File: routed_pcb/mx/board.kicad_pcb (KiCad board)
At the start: 2 copper layers, 100 x 100 mm, 28 parts

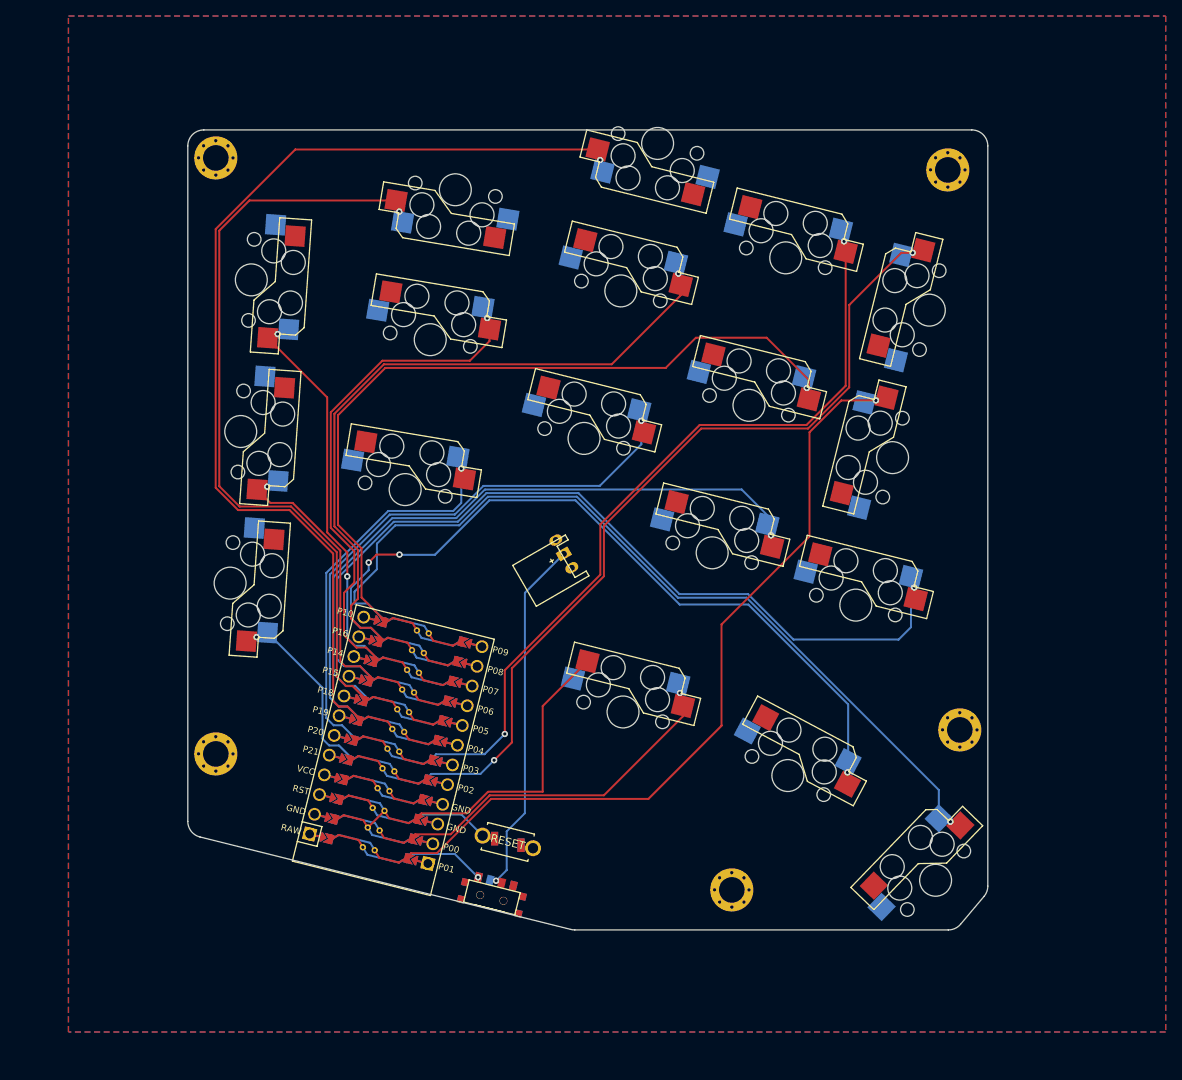
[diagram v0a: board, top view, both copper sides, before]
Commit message: choc v1.1 and mx v1.2
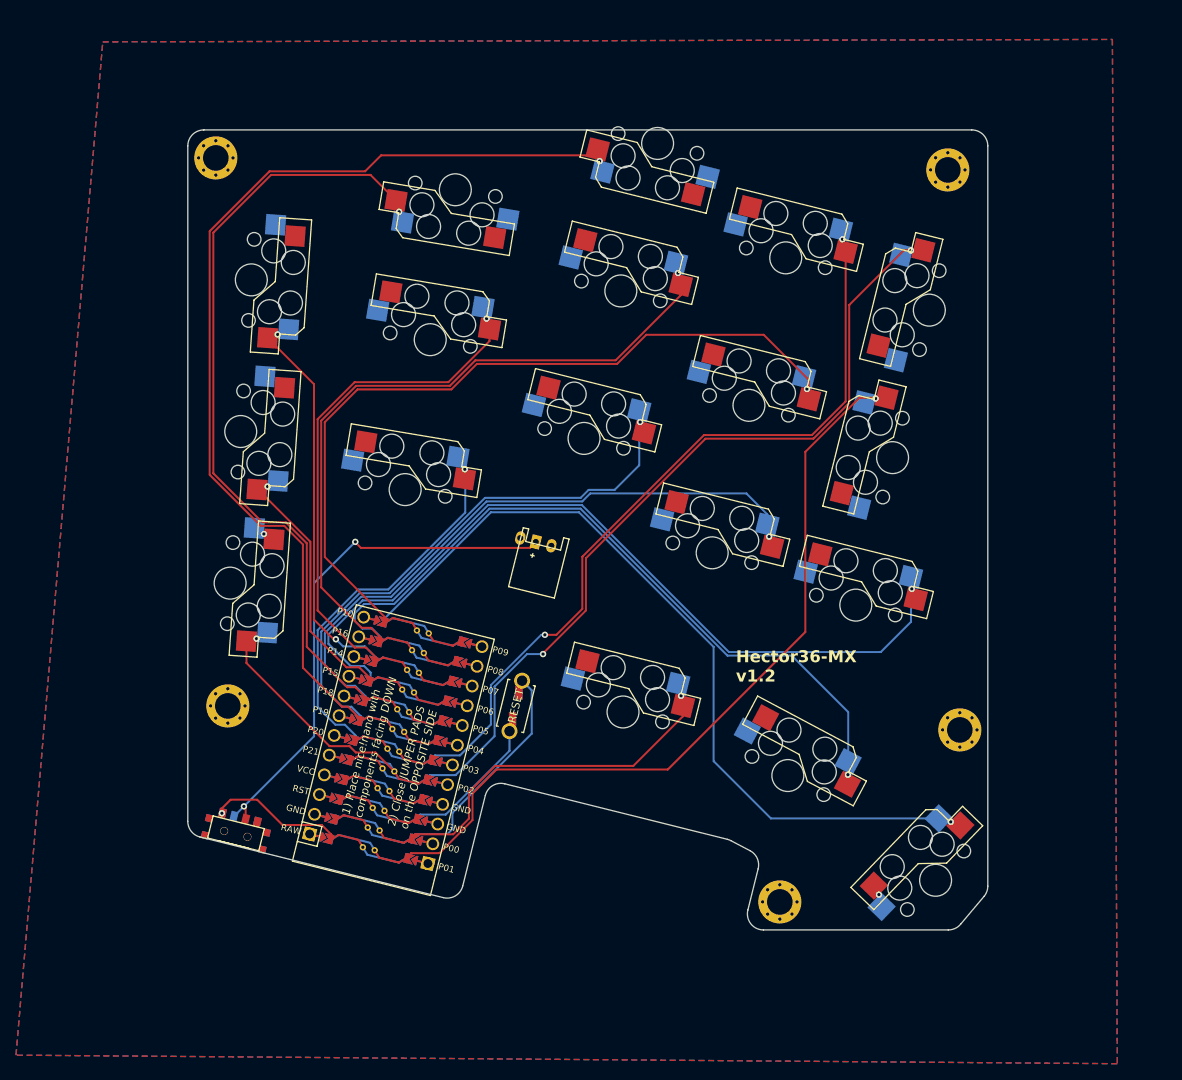
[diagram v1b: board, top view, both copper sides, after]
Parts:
- moved T1 33.0 mm to (89.5, 137.8)
- moved B1 17.0 mm to (124.5, 121.8), turned to -104 degrees
- moved B2 17.0 mm to (124.5, 121.8), turned to 76 degrees
- moved HOLE4 6.18 mm to (157.5, 146.3)
- moved HOLE5 6.18 mm to (88.5, 121.8)
- moved JST1 3.81 mm to (127.0, 101.3), turned to -14 degrees
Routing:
- net Bplus: track 46.0 -> 65.7 mm, vias 1 -> 2
- net GND: track 38.8 -> 28.8 mm, vias 0 -> 2
- net thumb_reachy: track 108.0 -> 99.5 mm
- net thumb_tucky: track 97.0 -> 89.5 mm, vias 3 -> 1
- net RAW: track 10.4 -> 17.1 mm
- net matrix_inner_bottom: track 109.5 -> 103.4 mm
- net matrix_index_bottom: track 82.2 -> 76.3 mm
- net matrix_pinky_home: track 35.7 -> 30.9 mm
- net RST: track 12.9 -> 17.7 mm
- net matrix_middle_top: track 128.3 -> 124.0 mm
- net matrix_index_top: track 99.6 -> 95.8 mm
- net matrix_middle_bottom: track 72.2 -> 69.2 mm
- net matrix_pinky_bottom: track 24.1 -> 26.8 mm
- net matrix_ring_bottom: track 51.0 -> 48.4 mm
- net matrix_ring_home: track 63.4 -> 61.2 mm
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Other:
- outline, holes or cut-outs redrawn
- board text added: "1) Place nice!nano with components facing DOWN"
- board text added: "2) Close JUMPER PADS on the OPPOSITE SIDE"
- board text added: "Hector36-MX v1.2"

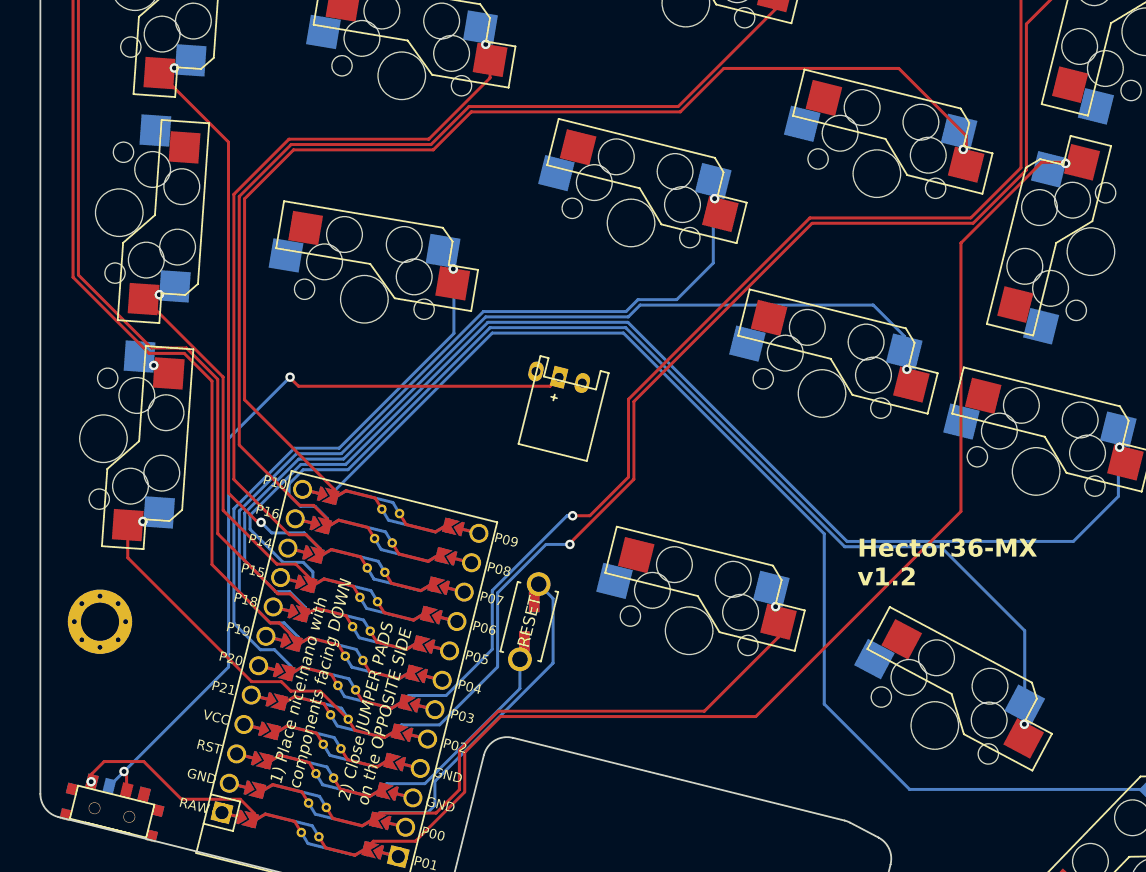
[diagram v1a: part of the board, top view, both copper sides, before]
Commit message: cleaned up text on mx, routed choc mx spacing
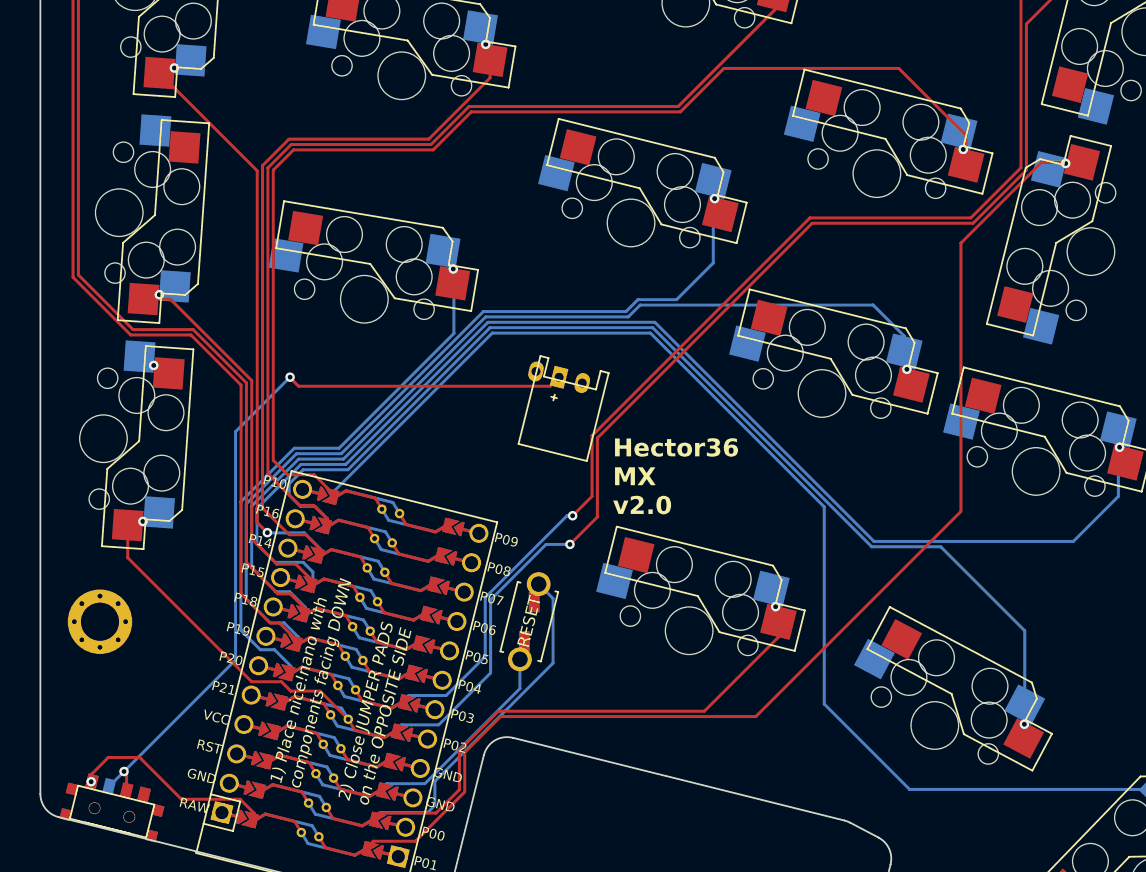
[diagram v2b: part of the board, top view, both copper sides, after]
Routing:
- net matrix_middle_home: track 84.2 -> 82.2 mm
- net matrix_ring_home: track 61.2 -> 59.2 mm
- net thumb_reachy: track 99.5 -> 100.8 mm
- net matrix_middle_top: track 124.0 -> 125.2 mm
- net matrix_ring_top: track 96.0 -> 97.2 mm
- net matrix_pinky_home: track 30.9 -> 32.1 mm
- net matrix_index_top: track 95.8 -> 95.0 mm
- net matrix_index_home: track 98.2 -> 97.5 mm
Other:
- board text added: "Hector36 MX v2.0"
- board text removed: "Hector36-MX v1.2"

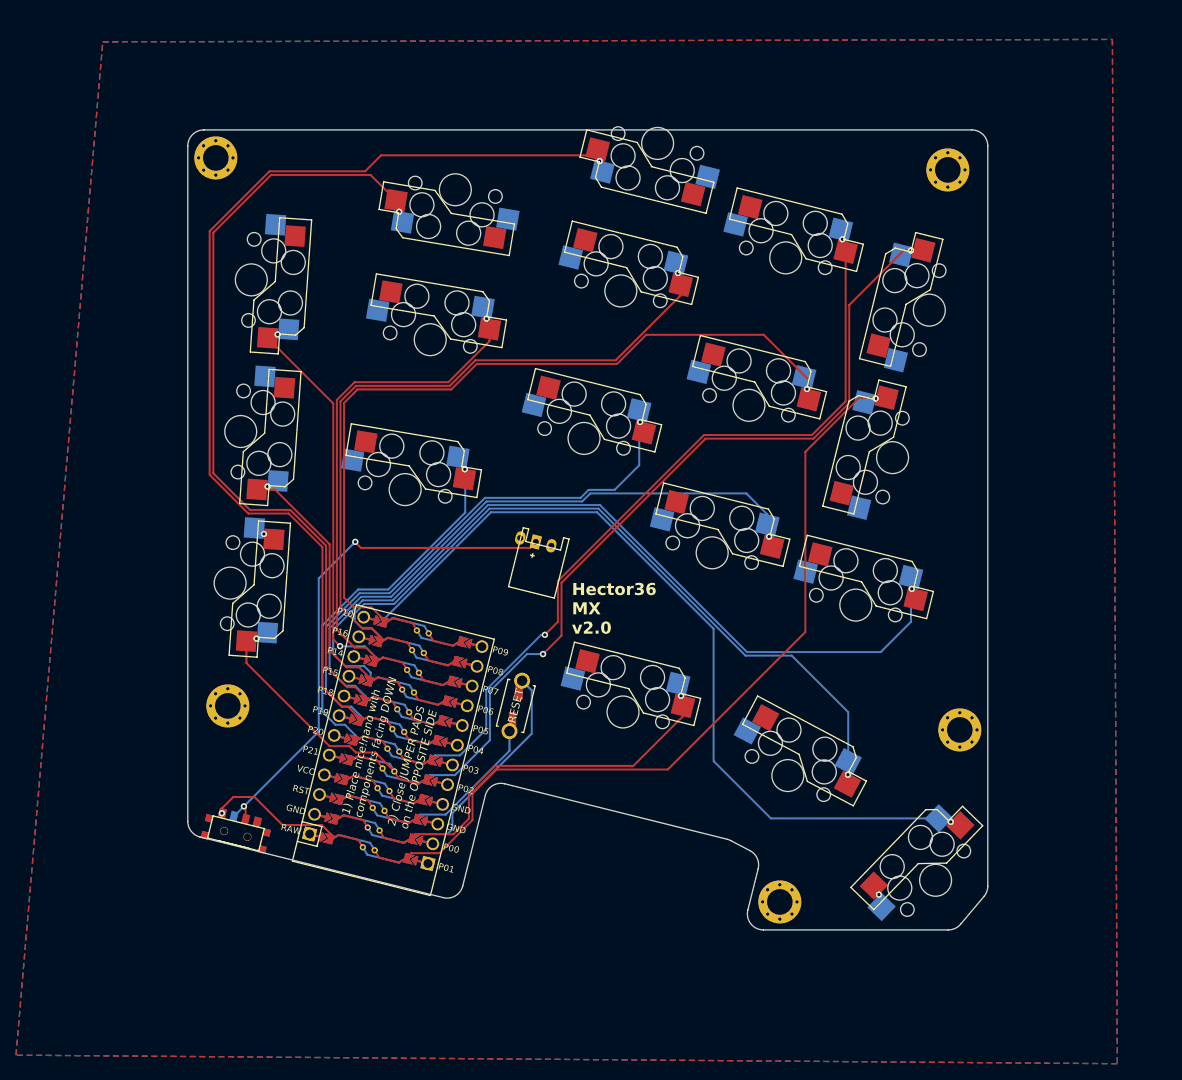
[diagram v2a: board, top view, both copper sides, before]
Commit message: modified mx switch orientation to be the same as all the other mx spacing versions
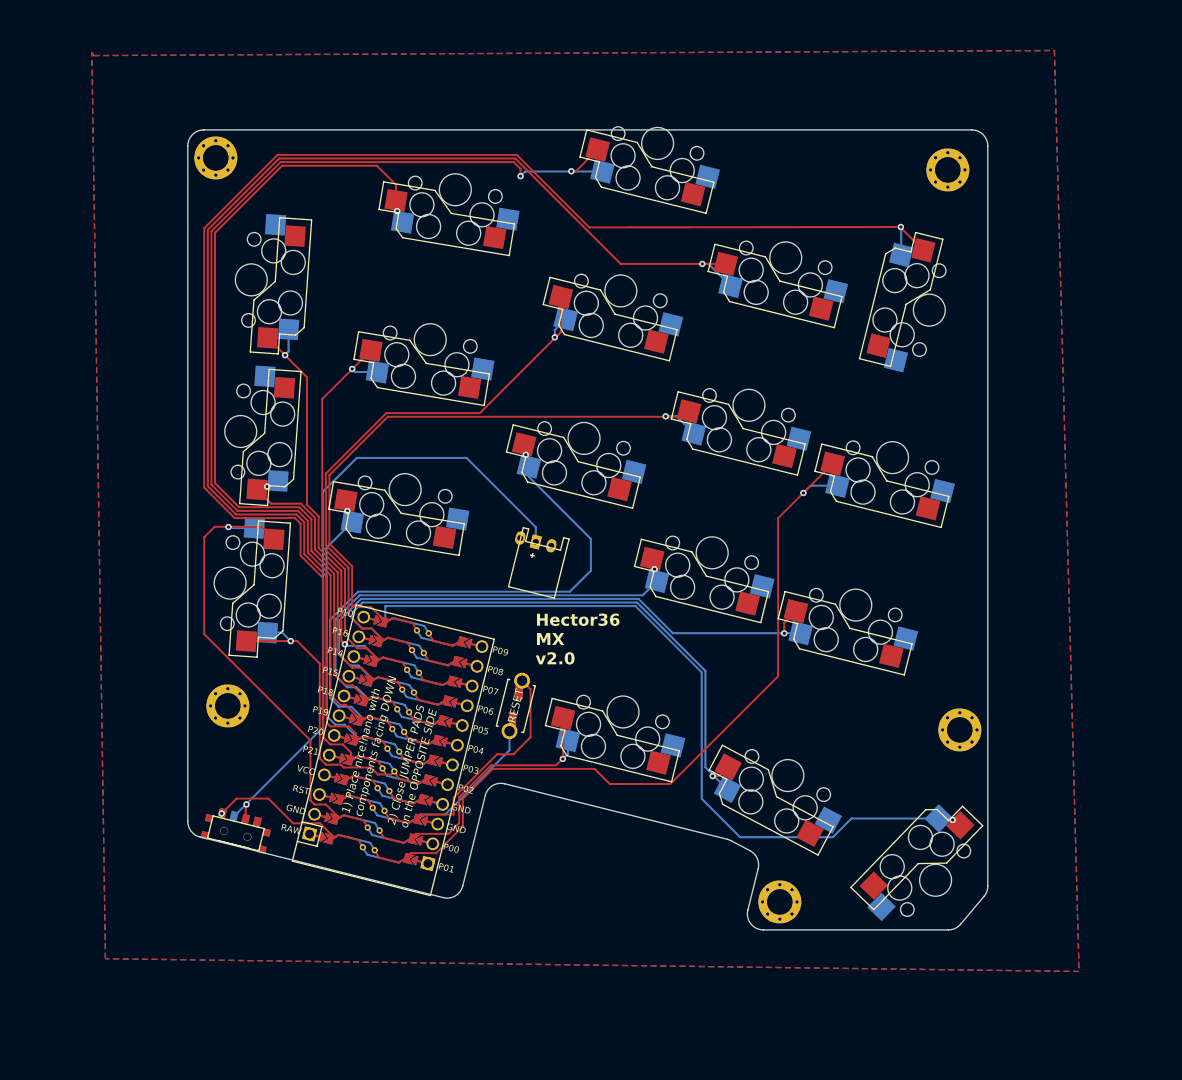
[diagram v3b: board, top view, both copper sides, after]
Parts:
- turned SW1 to 86 degrees
- turned SW14 to -14 degrees
- turned SW15 to -104 degrees
- turned SW18 to -134 degrees
- turned SW2 to 86 degrees
- turned SW3 to 86 degrees
- turned SW6 to -9.5 degrees
- turned SW9 to -14 degrees
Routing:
- net matrix_inner_top: track 104.5 -> 181.7 mm, vias 2 -> 1
- net matrix_index_top: track 95.0 -> 155.9 mm, vias 2 -> 1
- net GND: track 28.8 -> 83.5 mm, vias 2 -> 1
- net matrix_inner_bottom: track 103.4 -> 73.8 mm
- net matrix_index_home: track 97.5 -> 75.4 mm
- net matrix_index_bottom: track 75.8 -> 57.7 mm
- net thumb_tucky: track 89.5 -> 72.5 mm
- net Bplus: track 65.7 -> 80.9 mm, vias 2 -> 1
- net matrix_ring_bottom: track 47.9 -> 33.9 mm
- net matrix_middle_home: track 82.2 -> 68.6 mm
- net matrix_ring_home: track 59.2 -> 48.2 mm
- net thumb_inner: track 43.5 -> 32.7 mm
- net matrix_pinky_bottom: track 26.8 -> 35.9 mm
- net matrix_middle_top: track 125.2 -> 132.2 mm, vias 1 -> 2
- net matrix_ring_top: track 97.2 -> 103.4 mm
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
